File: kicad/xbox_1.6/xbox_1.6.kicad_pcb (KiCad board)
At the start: 4 copper layers, 179 parts, among them J1G1 jst_phd_12, J7G1 jst_phd_12, J8C1 IDC_40_Pin, Q3F1 SOT-23, U2C1 intel_495_bga2, U4B1 ddr_100_tqfp, U4C1 nvidia_xgpu_nv2a, U5F1 ddr_100_tqfp, U6D1 ddr_100_tqfp, U6E1 nvidia_mcpx

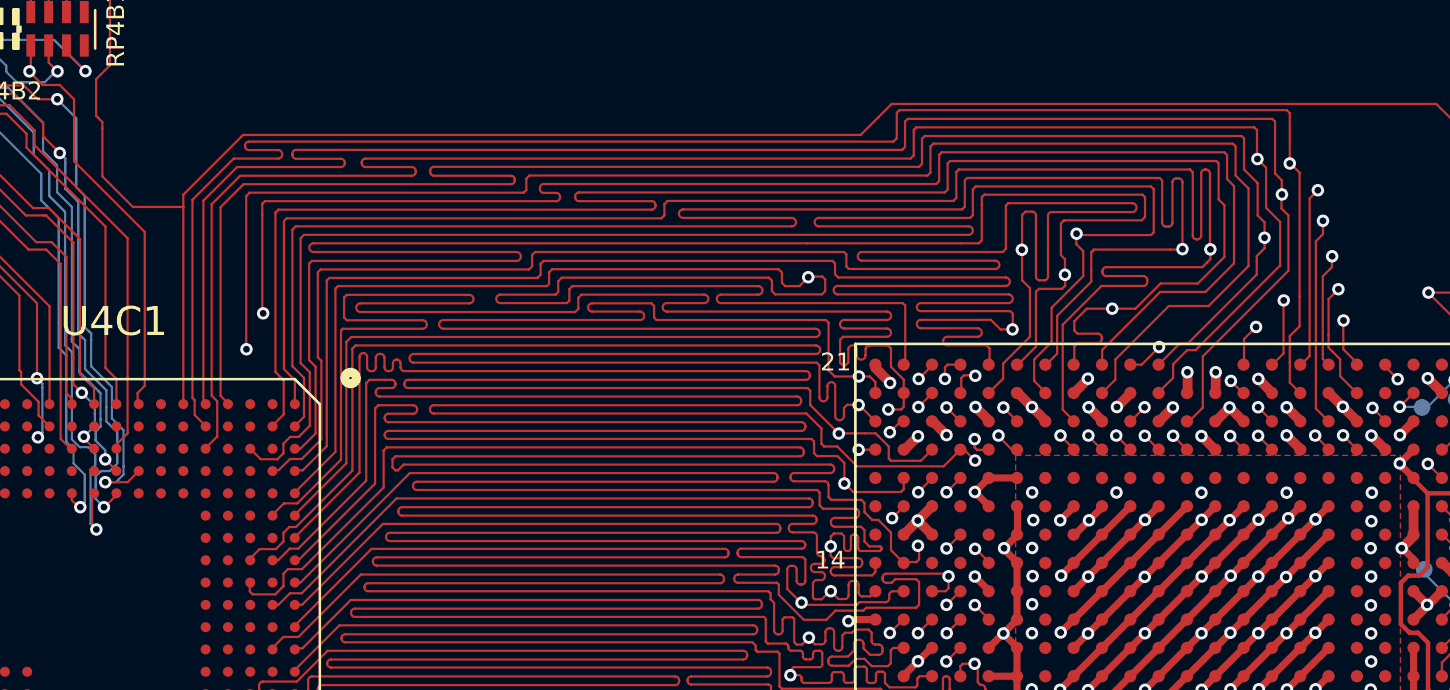
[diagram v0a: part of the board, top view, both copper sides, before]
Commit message: route more cpu signal on the back side
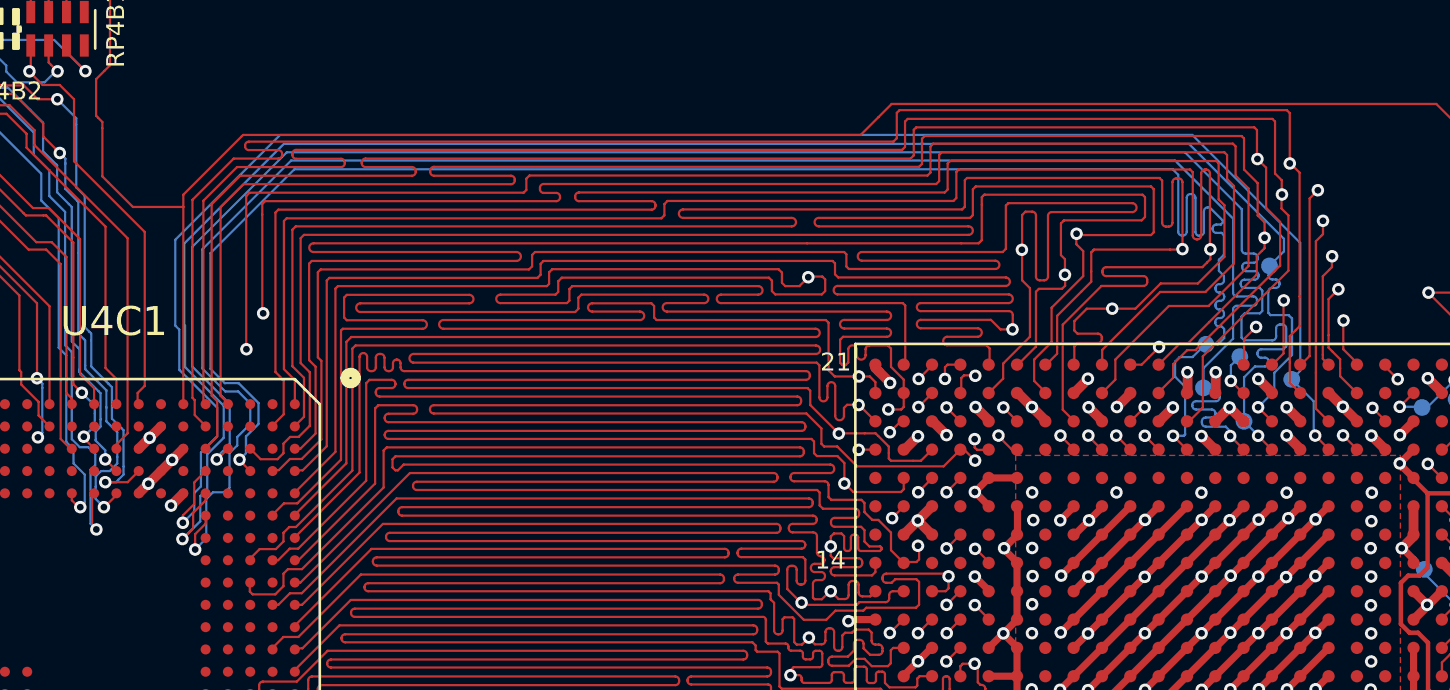
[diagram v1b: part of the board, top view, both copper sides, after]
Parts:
- added REF**: TP, xbox_footprint:TP, B.Cu at (276.9, 103.7)
- added REF**: TP, xbox_footprint:TP, B.Cu at (278.2, 99.6)
- added REF**: TP, xbox_footprint:TP, B.Cu at (279.2, 104.7)
- added REF**: TP, xbox_footprint:TP, B.Cu at (275.4, 103.2)
- added REF**: TP, xbox_footprint:TP, B.Cu at (275.2, 105.1)
- added REF**: TP, xbox_footprint:TP, B.Cu at (277.1, 106.6)
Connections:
- U4C1 pad AA20: (no net) -> /VSS
- U4C1 pad AA21: (no net) -> /VSS
- U4C1 pad AA22: (no net) -> /NB_VCC1
- U4C1 pad AB13: (no net) -> /NB_VCC1
- U4C1 pad AB15: (no net) -> /NB_VCC1
- U4C1 pad AB17: (no net) -> /NB_VCC1
- U4C1 pad AB19: (no net) -> /NB_VCC1
- U4C1 pad AB20: (no net) -> /VSS
- U4C1 pad AB21: (no net) -> /NB_VCC1
- U4C1 pad AB22: (no net) -> /VSS
- U4C1 pad C4: (no net) -> /CPU_D54
- U4C1 pad D3: (no net) -> /CPU_D63
- U4C1 pad E4: (no net) -> /CPU_D62
- U4C1 pad E5: (no net) -> /CPU_D56
- U4C1 pad E6: (no net) -> /CPU_D50
- U4C1 pad F3: (no net) -> /VSS
- U4C1 pad F5: (no net) -> /VSS
- U4C1 pad G2: (no net) -> /VSS
- U4C1 pad G4: (no net) -> /VSS
- U4C1 pad H3: (no net) -> /VSS
- U4C1 pad H5: (no net) -> /VSS
- U4C1 pad N14: (no net) -> /NB_VCC1
- U4C1 pad N16: (no net) -> /NB_VCC1
- U4C1 pad N18: (no net) -> /NB_VCC1
- U4C1 pad N19: (no net) -> /VSS
- U4C1 pad N20: (no net) -> /NB_VCC1
- U4C1 pad N21: (no net) -> /VSS
- U4C1 pad N22: (no net) -> /NB_VCC1
- U4C1 pad P13: (no net) -> /NB_VCC1
- U4C1 pad P19: (no net) -> /VSS
- U4C1 pad P20: (no net) -> /VSS
- U4C1 pad P21: (no net) -> /VSS
- U4C1 pad P22: (no net) -> /VSS
- U4C1 pad R19: (no net) -> /VSS
- U4C1 pad R20: (no net) -> /VSS
- U4C1 pad R21: (no net) -> /VSS
- U4C1 pad R22: (no net) -> /NB_VCC1
- U4C1 pad T13: (no net) -> /NB_VCC1
- U4C1 pad T19: (no net) -> /VSS
- U4C1 pad T20: (no net) -> /VSS
- U4C1 pad T21: (no net) -> /VSS
- U4C1 pad T22: (no net) -> /VSS
- U4C1 pad U19: (no net) -> /VSS
- U4C1 pad U20: (no net) -> /VSS
- U4C1 pad U21: (no net) -> /VSS
- U4C1 pad U22: (no net) -> /NB_VCC1
- U4C1 pad V13: (no net) -> /NB_VCC1
- U4C1 pad V19: (no net) -> /VSS
- U4C1 pad V20: (no net) -> /VSS
- U4C1 pad V21: (no net) -> /VSS
- U4C1 pad V22: (no net) -> /VSS
- U4C1 pad W20: (no net) -> /VSS
- U4C1 pad W21: (no net) -> /VSS
- U4C1 pad W22: (no net) -> /NB_VCC1
- U4C1 pad Y13: (no net) -> /NB_VCC1
- U4C1 pad Y20: (no net) -> /VSS
- U4C1 pad Y21: (no net) -> /VSS
- U4C1 pad Y22: (no net) -> /VSS
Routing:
- net /CPU_D50: track 0.86 -> 83.8 mm, vias 1 -> 2
- net /CPU_D63: track 0.88 -> 81.6 mm, vias 1 -> 2
- net /CPU_D62: track 0.88 -> 81.4 mm, vias 1 -> 2
- net /CPU_D54: track 0.88 -> 81.1 mm, vias 1 -> 2
- net /CPU_D56: track 0.89 -> 81.1 mm, vias 1 -> 2
- net /VSS: track 258.8 -> 263.8 mm, vias 156 -> 160
- net /CPU_DEP6: track 0.79 -> 2.05 mm

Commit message: route more cpu back
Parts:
- added REF**: TP, xbox_footprint:TP, B.Cu at (268.8, 105.4)
- added REF**: TP, xbox_footprint:TP, B.Cu at (233.2, 104.0)
- added REF**: TP, xbox_footprint:TP, B.Cu at (270.7, 105.3)
- added REF**: TP, xbox_footprint:TP, B.Cu at (265.8, 100.3)
- added REF**: TP, xbox_footprint:TP, B.Cu at (240.5, 98.4)
- added REF**: TP, xbox_footprint:TP, B.Cu at (269.3, 104.0)
- added REF**: TP, xbox_footprint:TP, B.Cu at (272.7, 97.3)
- added REF**: TP, xbox_footprint:TP, B.Cu at (233.0, 108.2)
- added REF**: TP, xbox_footprint:TP, B.Cu at (233.5, 100.5)
- added REF**: TP, xbox_footprint:TP, B.Cu at (273.2, 104.6)
- added REF**: TP, xbox_footprint:TP, B.Cu at (235.4, 98.8)
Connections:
- U4C1 pad B1: (no net) -> /VSS
- U4C1 pad C1: (no net) -> /CPU_D48
- U4C1 pad C2: (no net) -> /CPU_D41
- U4C1 pad C5: (no net) -> /CPU_D53
- U4C1 pad C6: (no net) -> /CPU_D46
- U4C1 pad C7: (no net) -> /CPU_D36
- U4C1 pad D5: (no net) -> /CPU_D57
- U4C1 pad D7: (no net) -> /CPU_D59
- U4C1 pad D9: (no net) -> /CPU_D37
- U4C1 pad E7: (no net) -> /CPU_D52
- U4C1 pad E8: (no net) -> /CPU_D40
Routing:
- net /CPU_D52: track 0.89 -> 83.6 mm, vias 1 -> 2
- net /CPU_D57: track 0.90 -> 79.6 mm, vias 1 -> 2
- net /CPU_D48: track 0.88 -> 78.5 mm, vias 1 -> 2
- net /CPU_D36: track 0.87 -> 76.3 mm, vias 1 -> 2
- net /CPU_D41: track 0.89 -> 76.1 mm, vias 1 -> 2
- net /CPU_D53: track 1.62 -> 76.5 mm, vias 1 -> 2
- net /CPU_D37: track 1.37 -> 76.2 mm, vias 1 -> 2
- net /CPU_D40: track 1.11 -> 75.8 mm, vias 1 -> 2
- net /CPU_D59: track 65.0 -> 78.6 mm, vias 1 -> 2
- net /CPU_D46: track 68.3 -> 78.4 mm, vias 1 -> 2
- net /VSS: track 263.8 -> 264.7 mm, vias 160 -> 161

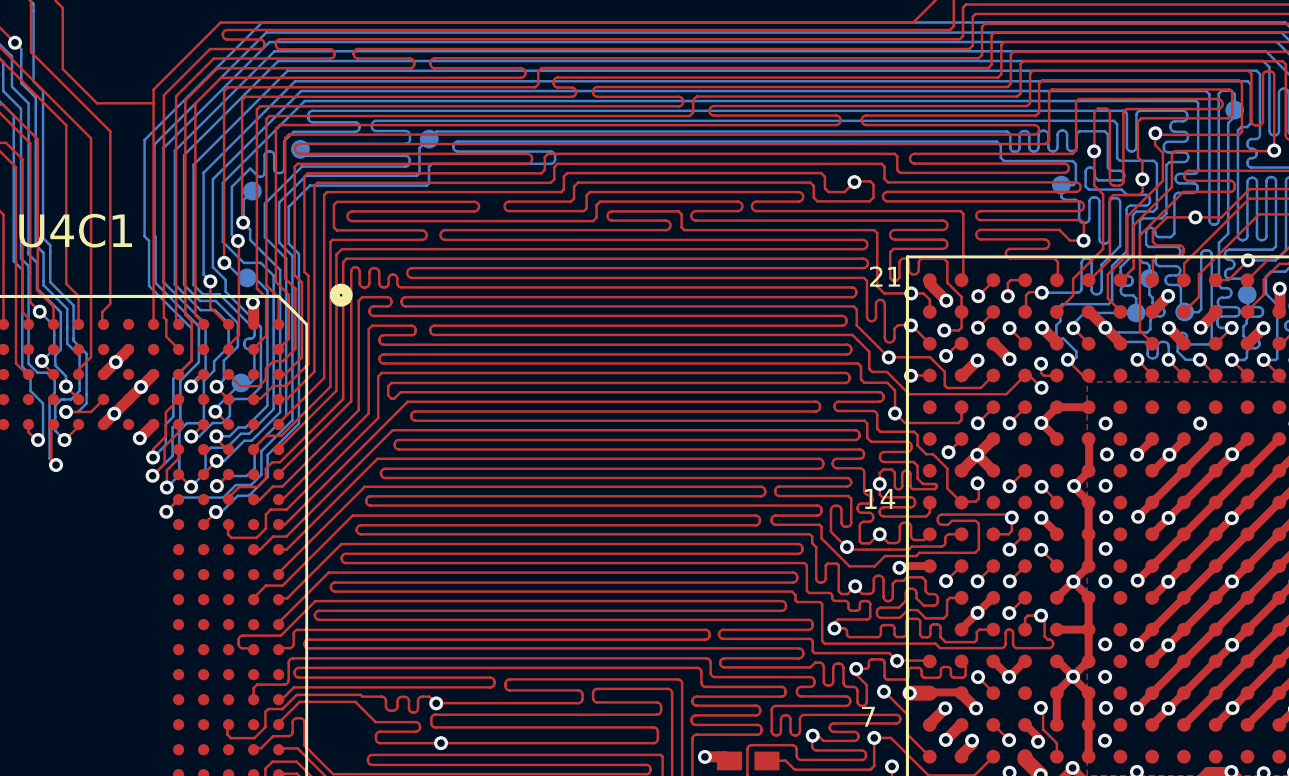
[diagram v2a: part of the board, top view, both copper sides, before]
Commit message: route more CPU traces
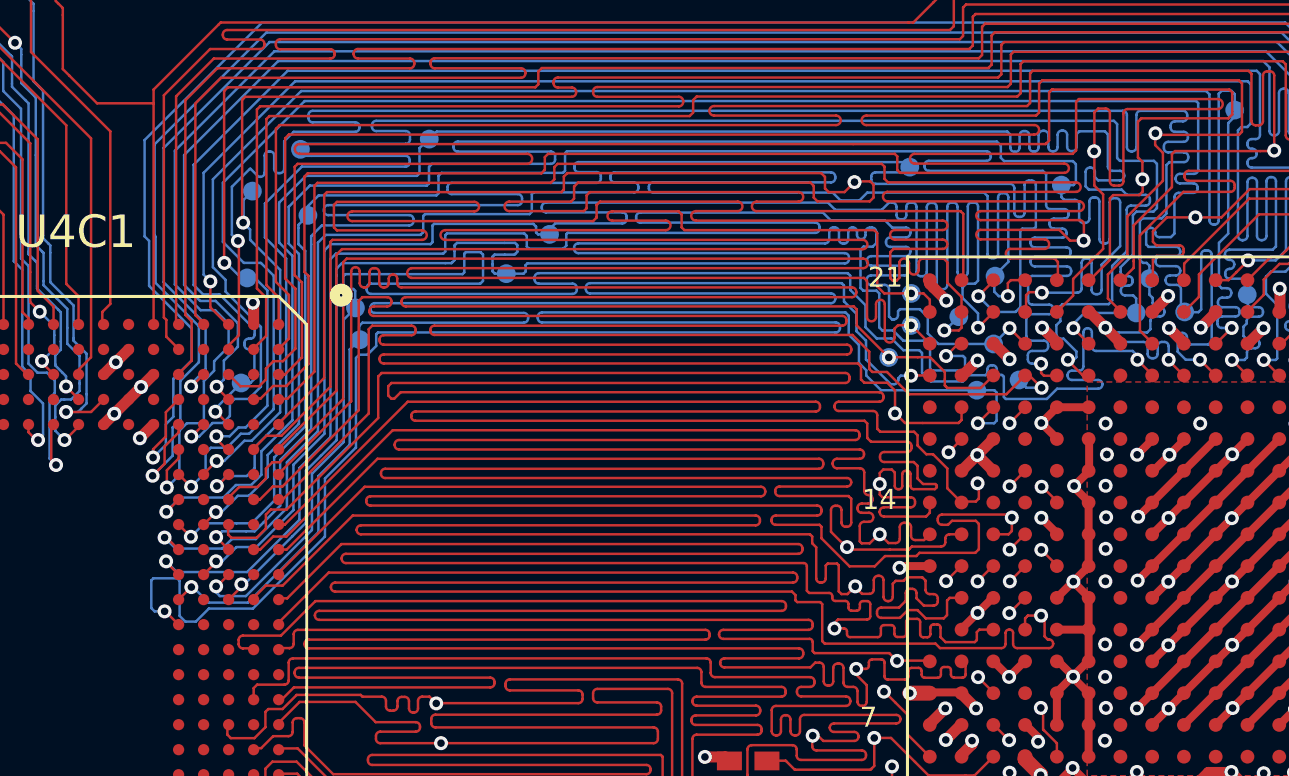
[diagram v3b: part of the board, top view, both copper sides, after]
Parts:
- added REF**: TP, xbox_footprint:TP, B.Cu at (261.7, 105.5)
- added REF**: TP, xbox_footprint:TP, B.Cu at (264.1, 108.0)
- added REF**: TP, xbox_footprint:TP, B.Cu at (237.8, 106.4)
- added REF**: TP, xbox_footprint:TP, B.Cu at (245.3, 102.2)
- added REF**: TP, xbox_footprint:TP, B.Cu at (258.9, 107.2)
- added REF**: TP, xbox_footprint:TP, B.Cu at (259.7, 99.5)
- added REF**: TP, xbox_footprint:TP, B.Cu at (263.1, 106.6)
- added REF**: TP, xbox_footprint:TP, B.Cu at (262.4, 108.5)
- added REF**: TP, xbox_footprint:TP, B.Cu at (237.6, 105.2)
- added REF**: TP, xbox_footprint:TP, B.Cu at (263.1, 103.9)
- added REF**: TP, xbox_footprint:TP, B.Cu at (243.6, 103.8)
- added REF**: TP, xbox_footprint:TP, B.Cu at (259.8, 104.6)
- added REF**: TP, xbox_footprint:TP, B.Cu at (259.8, 105.9)
- added REF**: TP, xbox_footprint:TP, B.Cu at (235.7, 101.5)
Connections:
- U4C1 pad C10: (no net) -> /CPU_D33
- U4C1 pad C11: (no net) -> /CPU_D39
- U4C1 pad C12: (no net) -> /CPU_D27
- U4C1 pad D11: (no net) -> /CPU_D35
- U4C1 pad E10: (no net) -> /CPU_D38
- U4C1 pad E11: (no net) -> /CPU_D32
- U4C1 pad E12: (no net) -> /CPU_D23
- U4C1 pad E13: (no net) -> /CPU_D24
- U4C1 pad E9: (no net) -> /CPU_D34
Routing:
- net /CPU_D27: track 0.82 -> 77.0 mm, vias 1 -> 2
- net /CPU_D32: track 0.88 -> 76.1 mm, vias 1 -> 2
- net /CPU_D24: track 0.90 -> 76.1 mm, vias 1 -> 2
- net /CPU_D35: track 0.88 -> 76.0 mm, vias 1 -> 2
- net /CPU_D23: track 0.75 -> 75.6 mm, vias 1 -> 2
- net /CPU_D39: track 0.87 -> 75.7 mm, vias 1 -> 2
- net /CPU_D38: track 1.26 -> 76.1 mm, vias 1 -> 2
- net /CPU_D33: track 0.89 -> 75.4 mm, vias 1 -> 2
- net /CPU_D34: track 1.05 -> 75.5 mm, vias 1 -> 2
- net /CPU_D28: track 75.2 -> 76.3 mm
- net /CPU_D29: track 75.0 -> 75.8 mm
